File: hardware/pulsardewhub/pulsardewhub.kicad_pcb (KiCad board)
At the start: 4 copper layers, 180 x 110 mm, 233 parts, among them J1 SWD, J10 XT60: 2=PLUS, 1=GND, J101 5A DC / center +, J11 BARREL input / DNP, J201 5A DC / center +, J301 5A DC / center +, J40 USB-C upstream, J401 5A DC / center +, J501 USB-A / 500mA, J51 HEATER 1, J601 USB-A / 500mA, J61 HEATER 2, J701 USB-A / 500mA, J801 USB-A / 500mA, Q10 SiR680LDP, Q11 SiR680LDP, Q51 AOD4184A, Q61 AOD4184A, U1 STM32G0B1KBU6, U10 LM74700QDBV, U101 TPS25974LRPW, U102 TVS1800DRV, U2 SHT40-AD1B-R2, U20 LMR33630ADDA, U201 TPS25974LRPW, U202 TVS1800DRV, U30 LMR33630ADDA, U301 TPS25974LRPW, U302 TVS1800DRV, U40 USB2517-JZX, U401 TPS25974LRPW, U402 TVS1800DRV, U41 TPS3808G33DBV, U42 USBLC6-2SC6, U50 TC4427AVOA713, U501 TPS2553DBV, U502 USBLC6-2SC6, U51 INA226, U601 TPS2553DBV, U602 USBLC6-2SC6, U70 TPS3700DDC, U701 TPS2553DBV, U702 USBLC6-2SC6, U71 SN74LVC08APW, U801 TPS2553DBV, U802 USBLC6-2SC6, Y40 24MHz / CL=12pF

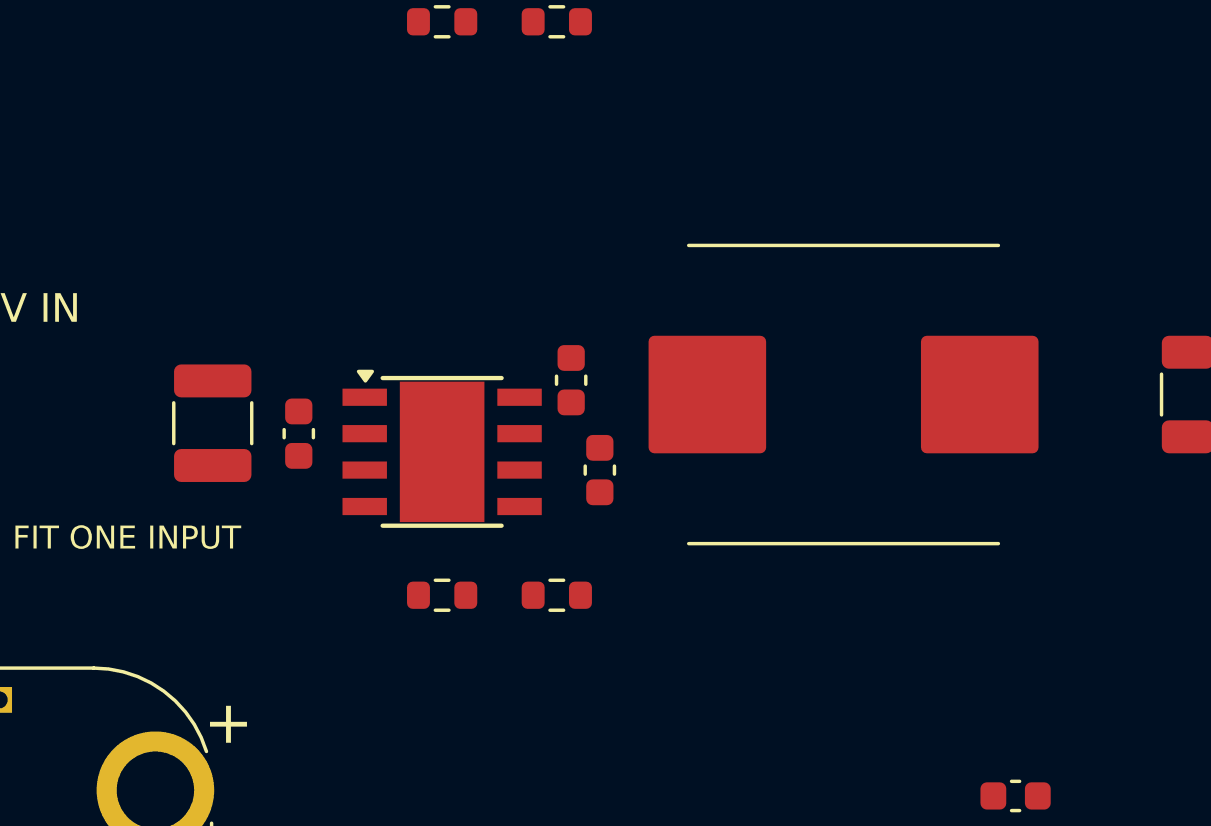
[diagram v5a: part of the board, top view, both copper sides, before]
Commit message: Use owned LMR51610 for PulsarPower 3.3 V logic supply
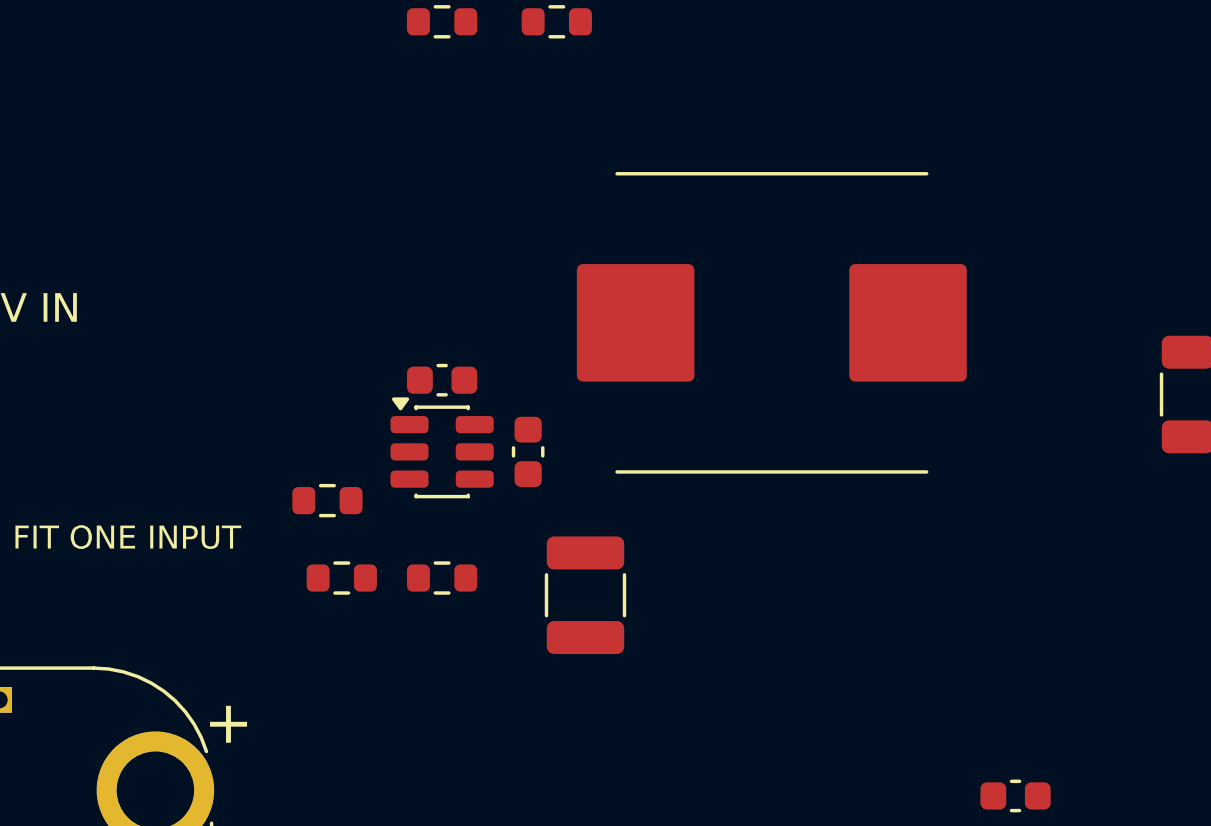
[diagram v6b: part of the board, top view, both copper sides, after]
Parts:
- removed C32: 1u / 50V, Capacitor_SMD:C_0603_1608Metric
- added R32: 12k, Resistor_SMD:R_0603_1608Metric, F.Cu at (76.0, 97.4)
- C31: value 220n / 50V -> 100n / 50V
- R31: value 43.2k -> 20k
- U30: value LMR33630ADDA -> LMR51610XDBVR; footprint Package_SO:Texas_HSOP-8-1EP_3.9x4.9mm_P1.27mm -> Package_TO_SOT_SMD:SOT-23-6
- moved C30 14.3 mm to (81.0, 98.0)
- moved R30 8.65 mm to (72.0, 94.7)
- moved C31 8.03 mm to (79.0, 93.0)
- moved C33 4.50 mm to (76.0, 90.5), turned to 0 degrees
- moved R31 3.55 mm to (72.5, 97.4)
- moved L30 3.54 mm to (87.5, 88.5)
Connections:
- C33 pad 1: Net-(U30-BOOT) -> Net-(U30-CB)
- R31 pad 2: /GND -> Net-(R31-Pad2)
- U30 pad 1: /GND -> Net-(U30-CB)
- U30 pad 2: /V5 -> /GND
- U30 pad 3: /V5 -> Net-(U30-FB)
- U30 pad 4: unconnected-(U30-PG-Pad4) -> /V5
- U30 pad 5: Net-(U30-FB) -> /V5
- U30 pad 6: Net-(U30-VCC) -> Net-(U30-SW)
